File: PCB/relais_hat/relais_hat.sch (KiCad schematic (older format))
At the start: 57 parts, among them J1 Conn_01x03, J10 Conn_01x02, J11 Conn_01x02, J12 Conn_01x03, J13 DB9_Female, J14 Conn_01x02, J2 Conn_01x03, J3 Conn_02x04_Odd_Even, J4 Screw_Terminal_01x02, J5 Screw_Terminal_01x02, J6 Screw_Terminal_01x02, J7 Screw_Terminal_01x02, J8 Conn_01x02, J9 Conn_01x02, K1 RELAY-HLS8L-DC3V-S-C(5P-19X15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, K2 RELAY-HLS8L-DC3V-S-C(5P-19X15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, K3 RELAY-HLS8L-DC3V-S-C(5P-19X15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, K4 RELAY-HLS8L-DC3V-S-C(5P-19X15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, P1 Conn_02x20_Odd_Even, Q1 S8050, Q2 S8050, Q3 S8050, Q4 S8050, U1 XC6206P302MR-G, U2 XC6206P302MR-G, U3 XC6206P302MR-G, U4 XC6206P302MR-G

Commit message: update/add LCSC ref and create fab file
bug for Res_hat with JLCPCB site
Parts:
- C1, C2, C3, C4: LCSC (none) -> C28323
- C5: LCSC (none) -> C311622
- D1, D2, D3, D4: LCSC (none) -> C375461
- D5, D6, D7, D8: LCSC (none) -> C60580
- Q1, Q2, Q3, Q4: LCSC (none) -> C2146
- R1, R2, R3, R4: LCSC (none) -> C17673
- R10, R11, R12, R9: LCSC (none) -> C102018
- R5, R6, R7, R8: LCSC (none) -> C17710
- U1, U2, U3, U4: LCSC (none) -> C5446
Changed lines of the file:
@@
 F 2 "Package_TO_SOT_SMD:SOT-23" H 4100 4125 50  0001 C CIN
 F 3 "https://www.torexsemi.com/file/xc6206/XC6206.pdf" H 4100 3900 50  0001 C CNN
+F 4 "C5446" H 4100 3900 50  0001 C CNN "LCSC"
 	1    4100 3900
 	1    0    0    -1
@@
 F 2 "Diode_SMD:D_SOD-123" H 4950 4075 50  0001 C CNN
 F 3 "https://assets.nexperia.com/documents/data-sheet/1N4148_1N4448.pdf" H 4950 4250 50  0001 C CNN
+F 4 "C60580" V 4950 4250 50  0001 C CNN "LCSC"
 	1    4950 4250
 	0    1    1    0
@@
 F 2 "Package_TO_SOT_SMD:SOT-23" H 5250 4825 50  0001 L CIN
 F 3 "http://www.unisonic.com.tw/datasheet/S8050.pdf" H 5050 4900 50  0001 L CNN
+F 4 "C2146" H 5050 4900 50  0001 C CNN "LCSC"
 	1    5050 4900
 	1    0    0    -1
@@
 F 2 "LED_SMD:LED_1206_3216Metric" H 4750 4350 50  0001 C CNN
 F 3 "~" H 4750 4350 50  0001 C CNN
+F 4 "C375461" V 4750 4350 50  0001 C CNN "LCSC"
 	1    4750 4350
 	0    -1   -1   0
@@
 F 2 "Resistor_SMD:R_0805_2012Metric" V 4630 4900 50  0001 C CNN
 F 3 "~" H 4700 4900 50  0001 C CNN
+F 4 "C17673" V 4700 4900 50  0001 C CNN "LCSC"
 	1    4700 4900
 	0    -1   -1   0
@@
 F 2 "Resistor_SMD:R_0805_2012Metric" V 4680 4050 50  0001 C CNN
 F 3 "~" H 4750 4050 50  0001 C CNN
+F 4 "C17710" V 4750 4050 50  0001 C CNN "LCSC"
 	1    4750 4050
 	1    0    0    -1
@@
 F 2 "Resistor_SMD:R_0805_2012Metric" V 4930 5300 50  0001 C CNN
 F 3 "~" H 5000 5300 50  0001 C CNN
+F 4 "C102018" V 5000 5300 50  0001 C CNN "LCSC"
 	1    5000 5300
 	0    -1   -1   0
@@
 F 2 "Capacitor_SMD:C_0805_2012Metric" H 4538 3900 50  0001 C CNN
 F 3 "~" H 4500 4050 50  0001 C CNN
+F 4 "C28323" V 4500 4050 50  0001 C CNN "LCSC"
 	1    4500 4050
 	1    0    0    -1
@@
 F 2 "Package_TO_SOT_SMD:SOT-23" H 1000 6275 50  0001 C CIN
 F 3 "https://www.torexsemi.com/file/xc6206/XC6206.pdf" H 1000 6050 50  0001 C CNN
+F 4 "C5446" H 1000 6050 50  0001 C CNN "LCSC"
 	1    1000 6050
 	1    0    0    -1
@@
 F 2 "Diode_SMD:D_SOD-123" H 1850 6225 50  0001 C CNN
 F 3 "https://assets.nexperia.com/documents/data-sheet/1N4148_1N4448.pdf" H 1850 6400 50  0001 C CNN
+F 4 "C60580" V 1850 6400 50  0001 C CNN "LCSC"
 	1    1850 6400
 	0    1    1    0
@@
 F 2 "Package_TO_SOT_SMD:SOT-23" H 2150 6975 50  0001 L CIN
 F 3 "http://www.unisonic.com.tw/datasheet/S8050.pdf" H 1950 7050 50  0001 L CNN
+F 4 "C2146" H 1950 7050 50  0001 C CNN "LCSC"
 	1    1950 7050
 	1    0    0    -1
@@
 F 2 "LED_SMD:LED_1206_3216Metric" H 1650 6500 50  0001 C CNN
 F 3 "~" H 1650 6500 50  0001 C CNN
+F 4 "C375461" V 1650 6500 50  0001 C CNN "LCSC"
 	1    1650 6500
 	0    -1   -1   0
@@
 F 2 "Resistor_SMD:R_0805_2012Metric" V 1530 7050 50  0001 C CNN
 F 3 "~" H 1600 7050 50  0001 C CNN
+F 4 "C17673" V 1600 7050 50  0001 C CNN "LCSC"
 	1    1600 7050
 	0    -1   -1   0
@@
 F 2 "Resistor_SMD:R_0805_2012Metric" V 1580 6200 50  0001 C CNN
 F 3 "~" H 1650 6200 50  0001 C CNN
+F 4 "C17710" V 1650 6200 50  0001 C CNN "LCSC"
 	1    1650 6200
 	1    0    0    -1
@@
 F 2 "Resistor_SMD:R_0805_2012Metric" V 1830 7450 50  0001 C CNN
 F 3 "~" H 1900 7450 50  0001 C CNN
+F 4 "C102018" V 1900 7450 50  0001 C CNN "LCSC"
 	1    1900 7450
 	0    -1   -1   0
@@
 F 2 "Capacitor_SMD:C_0805_2012Metric" H 1438 6050 50  0001 C CNN
 F 3 "~" H 1400 6200 50  0001 C CNN
+F 4 "C28323" V 1400 6200 50  0001 C CNN "LCSC"
 	1    1400 6200
 	1    0    0    -1
@@
 F 2 "Diode_SMD:D_SOD-123" H 1800 4275 50  0001 C CNN
 F 3 "https://assets.nexperia.com/documents/data-sheet/1N4148_1N4448.pdf" H 1800 4450 50  0001 C CNN
+F 4 "C60580" V 1800 4450 50  0001 C CNN "LCSC"
 	1    1800 4450
 	0    1    1    0
@@
 F 2 "Package_TO_SOT_SMD:SOT-23" H 2100 5025 50  0001 L CIN
 F 3 "http://www.unisonic.com.tw/datasheet/S8050.pdf" H 1900 5100 50  0001 L CNN
+F 4 "C2146" H 1900 5100 50  0001 C CNN "LCSC"
 	1    1900 5100
 	1    0    0    -1
@@
 F 2 "LED_SMD:LED_1206_3216Metric" H 1600 4550 50  0001 C CNN
 F 3 "~" H 1600 4550 50  0001 C CNN
+F 4 "C375461" V 1600 4550 50  0001 C CNN "LCSC"
 	1    1600 4550
 	0    -1   -1   0
@@
 F 2 "Resistor_SMD:R_0805_2012Metric" V 1480 5100 50  0001 C CNN
 F 3 "~" H 1550 5100 50  0001 C CNN
+F 4 "C17673" V 1550 5100 50  0001 C CNN "LCSC"
 	1    1550 5100
 	0    -1   -1   0
@@
 F 2 "Resistor_SMD:R_0805_2012Metric" V 1530 4250 50  0001 C CNN
 F 3 "~" H 1600 4250 50  0001 C CNN
+F 4 "C17710" V 1600 4250 50  0001 C CNN "LCSC"
 	1    1600 4250
 	1    0    0    -1
@@
 F 2 "Resistor_SMD:R_0805_2012Metric" V 1780 5500 50  0001 C CNN
 F 3 "~" H 1850 5500 50  0001 C CNN
+F 4 "C102018" V 1850 5500 50  0001 C CNN "LCSC"
 	1    1850 5500
 	0    -1   -1   0
@@
 F 2 "Capacitor_SMD:C_0805_2012Metric" H 1388 4100 50  0001 C CNN
 F 3 "~" H 1350 4250 50  0001 C CNN
+F 4 "C28323" V 1350 4250 50  0001 C CNN "LCSC"
 	1    1350 4250
 	1    0    0    -1
@@
 F 2 "Package_TO_SOT_SMD:SOT-23" H 4150 6375 50  0001 C CIN
 F 3 "https://www.torexsemi.com/file/xc6206/XC6206.pdf" H 4150 6150 50  0001 C CNN
+F 4 "C5446" H 4150 6150 50  0001 C CNN "LCSC"
 	1    4150 6150
 	1    0    0    -1
@@
 F 2 "Diode_SMD:D_SOD-123" H 5000 6325 50  0001 C CNN
 F 3 "https://assets.nexperia.com/documents/data-sheet/1N4148_1N4448.pdf" H 5000 6500 50  0001 C CNN
+F 4 "C60580" V 5000 6500 50  0001 C CNN "LCSC"
 	1    5000 6500
 	0    1    1    0
@@
 F 2 "Package_TO_SOT_SMD:SOT-23" H 5300 7075 50  0001 L CIN
 F 3 "http://www.unisonic.com.tw/datasheet/S8050.pdf" H 5100 7150 50  0001 L CNN
+F 4 "C2146" H 5100 7150 50  0001 C CNN "LCSC"
 	1    5100 7150
 	1    0    0    -1
@@
 F 2 "LED_SMD:LED_1206_3216Metric" H 4800 6600 50  0001 C CNN
 F 3 "~" H 4800 6600 50  0001 C CNN
+F 4 "C375461" V 4800 6600 50  0001 C CNN "LCSC"
 	1    4800 6600
 	0    -1   -1   0
@@
 F 2 "Resistor_SMD:R_0805_2012Metric" V 4680 7150 50  0001 C CNN
 F 3 "~" H 4750 7150 50  0001 C CNN
+F 4 "C17673" V 4750 7150 50  0001 C CNN "LCSC"
 	1    4750 7150
 	0    -1   -1   0
@@
 F 2 "Resistor_SMD:R_0805_2012Metric" V 4730 6300 50  0001 C CNN
 F 3 "~" H 4800 6300 50  0001 C CNN
+F 4 "C17710" V 4800 6300 50  0001 C CNN "LCSC"
 	1    4800 6300
 	1    0    0    -1
@@
 F 2 "Resistor_SMD:R_0805_2012Metric" V 4980 7550 50  0001 C CNN
 F 3 "~" H 5050 7550 50  0001 C CNN
+F 4 "C102018" V 5050 7550 50  0001 C CNN "LCSC"
 	1    5050 7550
 	0    -1   -1   0
@@
 F 2 "Capacitor_SMD:C_0805_2012Metric" H 4588 6150 50  0001 C CNN
 F 3 "~" H 4550 6300 50  0001 C CNN
+F 4 "C28323" V 4550 6300 50  0001 C CNN "LCSC"
 	1    4550 6300
 	1    0    0    -1
@@
 F 3 "~" H 8950 3850 50  0001 C CNN
 F 4 "EEE-FTH101XAV" H 8950 3850 50  0001 C CNN "Reference"
+F 5 "C311622" H 8950 3850 50  0001 C CNN "LCSC"
 	1    8950 3850
 	-1   0    0    1
@@
 F 2 "Package_TO_SOT_SMD:SOT-23" H 950 4325 50  0001 C CIN
 F 3 "https://www.torexsemi.com/file/xc6206/XC6206.pdf" H 950 4100 50  0001 C CNN
+F 4 "C5446" H 950 4100 50  0001 C CNN "LCSC"
 	1    950  4100
 	1    0    0    -1

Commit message: correct wrong ref for JLCPCB
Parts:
- D5, D6, D7, D8: LCSC C60580 -> C83528
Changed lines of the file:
@@
 F 2 "Diode_SMD:D_SOD-123" H 4950 4075 50  0001 C CNN
 F 3 "https://assets.nexperia.com/documents/data-sheet/1N4148_1N4448.pdf" H 4950 4250 50  0001 C CNN
-F 4 "C60580" V 4950 4250 50  0001 C CNN "LCSC"
+F 4 "C83528" V 4950 4250 50  0001 C CNN "LCSC"
 	1    4950 4250
 	0    1    1    0
@@
 F 2 "Diode_SMD:D_SOD-123" H 1850 6225 50  0001 C CNN
 F 3 "https://assets.nexperia.com/documents/data-sheet/1N4148_1N4448.pdf" H 1850 6400 50  0001 C CNN
-F 4 "C60580" V 1850 6400 50  0001 C CNN "LCSC"
+F 4 "C83528" V 1850 6400 50  0001 C CNN "LCSC"
 	1    1850 6400
 	0    1    1    0
@@
 F 2 "Diode_SMD:D_SOD-123" H 1800 4275 50  0001 C CNN
 F 3 "https://assets.nexperia.com/documents/data-sheet/1N4148_1N4448.pdf" H 1800 4450 50  0001 C CNN
-F 4 "C60580" V 1800 4450 50  0001 C CNN "LCSC"
+F 4 "C83528" V 1800 4450 50  0001 C CNN "LCSC"
 	1    1800 4450
 	0    1    1    0
@@
 F 2 "Diode_SMD:D_SOD-123" H 5000 6325 50  0001 C CNN
 F 3 "https://assets.nexperia.com/documents/data-sheet/1N4148_1N4448.pdf" H 5000 6500 50  0001 C CNN
-F 4 "C60580" V 5000 6500 50  0001 C CNN "LCSC"
+F 4 "C83528" V 5000 6500 50  0001 C CNN "LCSC"
 	1    5000 6500
 	0    1    1    0

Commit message: Q1/2/3/4 orientation correction
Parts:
- removed Q1, Q2, Q3, Q4: S8050, Package_TO_SOT_SMD:SOT-23, symbol Transistor_BJT:S8050
- added Q1, Q2, Q3, Q4: S8050, Package_TO_SOT_SMD:SOT-23, symbol Device:Q_NPN_BEC
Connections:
- net GND: now also Q1.2 (E), Q2.2 (E), Q3.2 (E), Q4.2 (E)
- net at D2.1 (K), D6.2 (A), K2.3 (V-): now also Q2.3 (C)
- net at R10.1, R2.2: now also Q2.1 (B)
- net at D3.1 (K), D7.2 (A), K3.3 (V-): now also Q3.3 (C)
- net at R11.1, R3.2: now also Q3.1 (B)
- net at D1.1 (K), D5.2 (A), K1.3 (V-): now also Q1.3 (C)
- net at R1.2, R9.1: now also Q1.1 (B)
- net at D4.1 (K), D8.2 (A), K4.3 (V-): now also Q4.3 (C)
- net at R12.1, R4.2: now also Q4.1 (B)
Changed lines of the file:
@@
-$EndComp
-$Comp
-L Transistor_BJT:S8050 Q2
-U 1 1 5E811C4B
-P 5050 4900
-F 0 "Q2" H 5240 4946 50  0000 L CNN
-F 1 "S8050" H 5240 4855 50  0000 L CNN
-F 2 "Package_TO_SOT_SMD:SOT-23" H 5250 4825 50  0001 L CIN
-F 3 "http://www.unisonic.com.tw/datasheet/S8050.pdf" H 5050 4900 50  0001 L CNN
-F 4 "C2146" H 5050 4900 50  0001 C CNN "LCSC"
-	1    5050 4900
-	1    0    0    -1
 $EndComp
 $Comp
@@
 	0    -1   -1   0
 $EndComp
-Connection ~ 4850 4900
 Connection ~ 5150 5300
 Wire Wire Line
@@
 $EndComp
 $Comp
-L Transistor_BJT:S8050 Q3
-U 1 1 5E87E470
-P 1950 7050
-F 0 "Q3" H 2140 7096 50  0000 L CNN
-F 1 "S8050" H 2140 7005 50  0000 L CNN
-F 2 "Package_TO_SOT_SMD:SOT-23" H 2150 6975 50  0001 L CIN
-F 3 "http://www.unisonic.com.tw/datasheet/S8050.pdf" H 1950 7050 50  0001 L CNN
-F 4 "C2146" H 1950 7050 50  0001 C CNN "LCSC"
-	1    1950 7050
-	1    0    0    -1
-$EndComp
-$Comp
 L Device:LED D3
 U 1 1 5E87E476
@@
 	0    -1   -1   0
 $EndComp
-Connection ~ 1750 7050
 Connection ~ 2050 7450
 Wire Wire Line
@@
 $EndComp
 $Comp
-L Transistor_BJT:S8050 Q1
-U 1 1 5E88AACF
-P 1900 5100
-F 0 "Q1" H 2090 5146 50  0000 L CNN
-F 1 "S8050" H 2090 5055 50  0000 L CNN
-F 2 "Package_TO_SOT_SMD:SOT-23" H 2100 5025 50  0001 L CIN
-F 3 "http://www.unisonic.com.tw/datasheet/S8050.pdf" H 1900 5100 50  0001 L CNN
-F 4 "C2146" H 1900 5100 50  0001 C CNN "LCSC"
-	1    1900 5100
-	1    0    0    -1
-$EndComp
-$Comp
 L Device:LED D1
 U 1 1 5E88AAD5
@@
 	0    -1   -1   0
 $EndComp
-Connection ~ 1700 5100
 Connection ~ 2000 5500
 Wire Wire Line
@@
 $EndComp
 $Comp
-L Transistor_BJT:S8050 Q4
-U 1 1 5E892F1E
-P 5100 7150
-F 0 "Q4" H 5290 7196 50  0000 L CNN
-F 1 "S8050" H 5290 7105 50  0000 L CNN
-F 2 "Package_TO_SOT_SMD:SOT-23" H 5300 7075 50  0001 L CIN
-F 3 "http://www.unisonic.com.tw/datasheet/S8050.pdf" H 5100 7150 50  0001 L CNN
-F 4 "C2146" H 5100 7150 50  0001 C CNN "LCSC"
-	1    5100 7150
-	1    0    0    -1
-$EndComp
-$Comp
 L Device:LED D4
 U 1 1 5E892F24
@@
 	0    -1   -1   0
 $EndComp
-Connection ~ 4900 7150
 Connection ~ 5200 7550
 Wire Wire Line
@@
 Text Label 4900 2300 2    50   ~ 0
 rpi_gnd
+$Comp
+L Device:Q_NPN_BEC Q1
+U 1 1 5F7C630D
+P 1900 5100
+F 0 "Q1" H 2090 5146 50  0000 L CNN
+F 1 "S8050" H 2090 5055 50  0000 L CNN
+F 2 "Package_TO_SOT_SMD:SOT-23" H 2100 5200 50  0001 C CNN
+F 3 "~" H 1900 5100 50  0001 C CNN
+	1    1900 5100
+	1    0    0    -1
+$EndComp
+$Comp
+L Device:Q_NPN_BEC Q3
+U 1 1 5F7C7DFB
+P 1950 7050
+F 0 "Q3" H 2140 7096 50  0000 L CNN
+F 1 "S8050" H 2140 7005 50  0000 L CNN
+F 2 "Package_TO_SOT_SMD:SOT-23" H 2150 7150 50  0001 C CNN
+F 3 "~" H 1950 7050 50  0001 C CNN
+	1    1950 7050
+	1    0    0    -1
+$EndComp
+$Comp
+L Device:Q_NPN_BEC Q2
+U 1 1 5F7CC619
+P 5050 4900
+F 0 "Q2" H 5240 4946 50  0000 L CNN
+F 1 "S8050" H 5240 4855 50  0000 L CNN
+F 2 "Package_TO_SOT_SMD:SOT-23" H 5250 5000 50  0001 C CNN
+F 3 "~" H 5050 4900 50  0001 C CNN
+	1    5050 4900
+	1    0    0    -1
+$EndComp
+Connection ~ 1700 5100
+$Comp
+L Device:Q_NPN_BEC Q4
+U 1 1 5F7D1148
+P 5100 7150
+F 0 "Q4" H 5290 7196 50  0000 L CNN
+F 1 "S8050" H 5290 7105 50  0000 L CNN
+F 2 "Package_TO_SOT_SMD:SOT-23" H 5300 7250 50  0001 C CNN
+F 3 "~" H 5100 7150 50  0001 C CNN
+	1    5100 7150
+	1    0    0    -1
+$EndComp
+Connection ~ 4900 7150
+Connection ~ 1750 7050
+Connection ~ 4850 4900
 $EndSCHEMATC

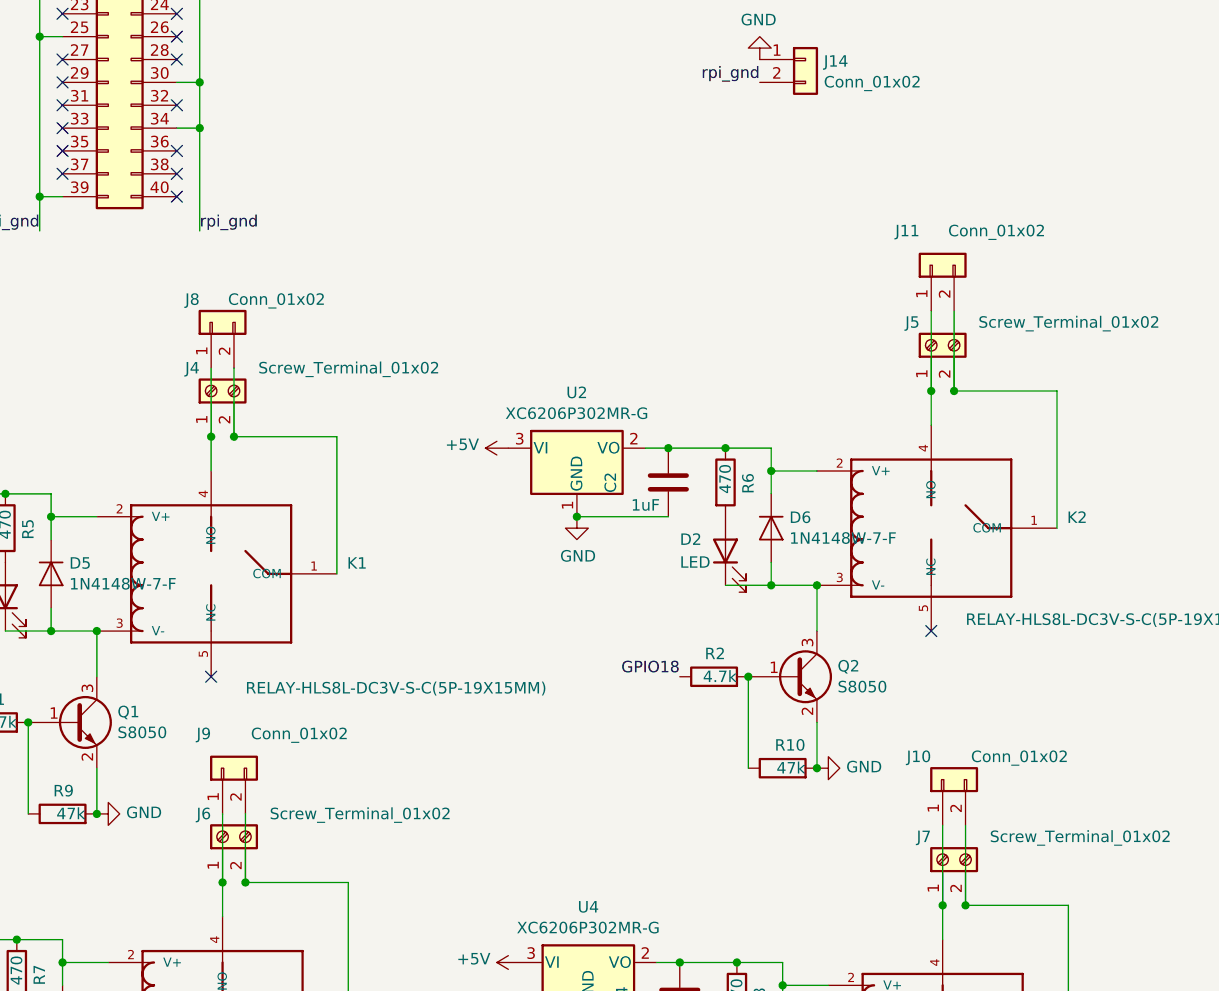
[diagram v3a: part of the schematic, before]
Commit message: update alim and relais pcb 2-> 4 couches
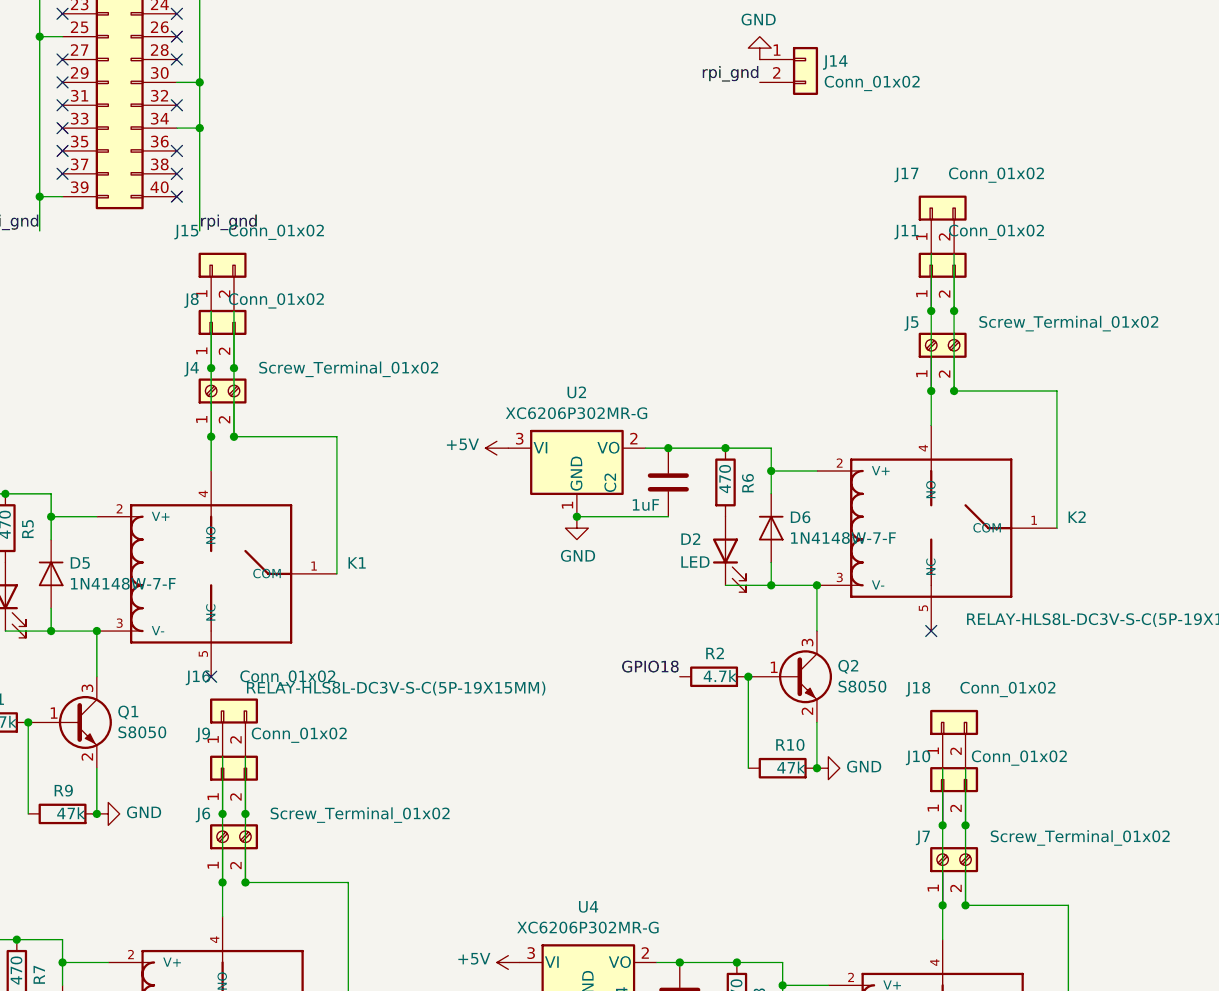
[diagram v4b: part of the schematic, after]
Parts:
- added J15, J16, J17, J18: Conn_01x02, Connector_PinHeader_2.54mm:PinHeader_1x02_P2.54mm_Vertical, symbol Connector_Generic:Conn_01x02
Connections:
- net at J6.1 (Pin_1), J9.1 (Pin_1), K3.4 (NO): now also J16.1 (Pin_1)
- net at J6.2 (Pin_2), J9.2 (Pin_2), K3.1 (COM): now also J16.2 (Pin_2)
- net at J4.1 (Pin_1), J8.1 (Pin_1), K1.4 (NO): now also J15.1 (Pin_1)
- net at J4.2 (Pin_2), J8.2 (Pin_2), K1.1 (COM): now also J15.2 (Pin_2)
- net at J10.1 (Pin_1), J7.1 (Pin_1), K4.4 (NO): now also J18.1 (Pin_1)
- net at J10.2 (Pin_2), J7.2 (Pin_2), K4.1 (COM): now also J18.2 (Pin_2)
- net at J11.1 (Pin_1), J5.1 (Pin_1), K2.4 (NO): now also J17.1 (Pin_1)
- net at J11.2 (Pin_2), J5.2 (Pin_2), K2.1 (COM): now also J17.2 (Pin_2)
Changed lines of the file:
@@
 Connection ~ 1750 7050
 Connection ~ 4850 4900
+$Comp
+L Connector_Generic:Conn_01x02 J?
+U 1 1 5FAB551C
+P 5650 2850
+AR Path="/5E5C0CC9/5FAB551C" Ref="J?"  Part="1"
+AR Path="/5FAB551C" Ref="J17"  Part="1"
+F 0 "J17" V 5800 2900 50  0000 L CNN
+F 1 "Conn_01x02" V 5800 2350 50  0000 L CNN
+F 2 "Connector_PinHeader_2.54mm:PinHeader_1x02_P2.54mm_Vertical" H 5650 2850 50  0001 C CNN
+F 3 "~" H 5650 2850 50  0001 C CNN
+	1    5650 2850
+	0    -1   -1   0
+$EndComp
+$Comp
+L Connector_Generic:Conn_01x02 J?
+U 1 1 5FAB9E19
+P 2500 3100
+AR Path="/5E5C0CC9/5FAB9E19" Ref="J?"  Part="1"
+AR Path="/5FAB9E19" Ref="J15"  Part="1"
+F 0 "J15" V 2650 3150 50  0000 L CNN
+F 1 "Conn_01x02" V 2650 2600 50  0000 L CNN
+F 2 "Connector_PinHeader_2.54mm:PinHeader_1x02_P2.54mm_Vertical" H 2500 3100 50  0001 C CNN
+F 3 "~" H 2500 3100 50  0001 C CNN
+	1    2500 3100
+	0    -1   -1   0
+$EndComp
+$Comp
+L Connector_Generic:Conn_01x02 J?
+U 1 1 5FABE8AB
+P 2550 5050
+AR Path="/5E5C0CC9/5FABE8AB" Ref="J?"  Part="1"
+AR Path="/5FABE8AB" Ref="J16"  Part="1"
+F 0 "J16" V 2700 5100 50  0000 L CNN
+F 1 "Conn_01x02" V 2700 4550 50  0000 L CNN
+F 2 "Connector_PinHeader_2.54mm:PinHeader_1x02_P2.54mm_Vertical" H 2550 5050 50  0001 C CNN
+F 3 "~" H 2550 5050 50  0001 C CNN
+	1    2550 5050
+	0    -1   -1   0
+$EndComp
+$Comp
+L Connector_Generic:Conn_01x02 J?
+U 1 1 5FAC338D
+P 5700 5100
+AR Path="/5E5C0CC9/5FAC338D" Ref="J?"  Part="1"
+AR Path="/5FAC338D" Ref="J18"  Part="1"
+F 0 "J18" V 5850 5150 50  0000 L CNN
+F 1 "Conn_01x02" V 5850 4600 50  0000 L CNN
+F 2 "Connector_PinHeader_2.54mm:PinHeader_1x02_P2.54mm_Vertical" H 5700 5100 50  0001 C CNN
+F 3 "~" H 5700 5100 50  0001 C CNN
+	1    5700 5100
+	0    -1   -1   0
+$EndComp
+Wire Wire Line
+	5650 3300 5650 3050
+Connection ~ 5650 3300
+Wire Wire Line
+	5750 3300 5750 3050
+Connection ~ 5750 3300
+Wire Wire Line
+	2500 3550 2500 3300
+Connection ~ 2500 3550
+Wire Wire Line
+	2600 3550 2600 3300
+Connection ~ 2600 3550
+Wire Wire Line
+	2550 5500 2550 5250
+Connection ~ 2550 5500
+Wire Wire Line
+	2650 5250 2650 5500
+Connection ~ 2650 5500
+Wire Wire Line
+	5700 5300 5700 5550
+Connection ~ 5700 5550
+Wire Wire Line
+	5800 5300 5800 5550
+Connection ~ 5800 5550
 $EndSCHEMATC

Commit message: update 3d model and fab file for all board
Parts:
- MK1, MK2, MK3, MK4: value M2.5 -> M3
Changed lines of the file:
@@
 P 4750 1050
 F 0 "MK1" H 4850 1096 50  0000 L CNN
-F 1 "M2.5" H 4850 1005 50  0000 L CNN
+F 1 "M3" H 4850 1005 50  0000 L CNN
 F 2 "MountingHole:MountingHole_2.7mm_M2.5" H 4750 1050 60  0001 C CNN
 F 3 "" H 4750 1050 60  0001 C CNN
@@
 P 5150 1050
 F 0 "MK3" H 5250 1096 50  0000 L CNN
-F 1 "M2.5" H 5250 1005 50  0000 L CNN
+F 1 "M3" H 5250 1005 50  0000 L CNN
 F 2 "MountingHole:MountingHole_2.7mm_M2.5" H 5150 1050 60  0001 C CNN
 F 3 "" H 5150 1050 60  0001 C CNN
@@
 P 4750 1250
 F 0 "MK2" H 4850 1296 50  0000 L CNN
-F 1 "M2.5" H 4850 1205 50  0000 L CNN
+F 1 "M3" H 4850 1205 50  0000 L CNN
 F 2 "MountingHole:MountingHole_2.7mm_M2.5" H 4750 1250 60  0001 C CNN
 F 3 "" H 4750 1250 60  0001 C CNN
@@
 P 5150 1250
 F 0 "MK4" H 5250 1296 50  0000 L CNN
-F 1 "M2.5" H 5250 1205 50  0000 L CNN
+F 1 "M3" H 5250 1205 50  0000 L CNN
 F 2 "MountingHole:MountingHole_2.7mm_M2.5" H 5150 1250 60  0001 C CNN
 F 3 "" H 5150 1250 60  0001 C CNN
